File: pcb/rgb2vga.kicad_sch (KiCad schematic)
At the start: 40 parts, among them J1 GPIO_0, J2 RGB_IN, J3 COCO3_RGB_IN, J4 C_VIDEO_IN, J5 GPIO_1, J6 VGA_OUT, J7 Conn_01x03_Male, SW1 SW_DIP_x10, SW2 SW_DP3T, U1 LM1881

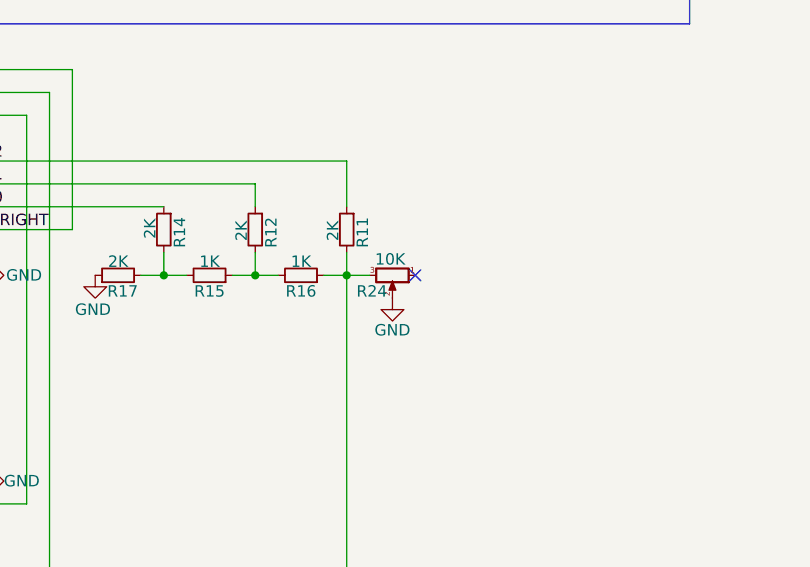
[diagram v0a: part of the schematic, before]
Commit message: multi-turn DAC trimmer pot
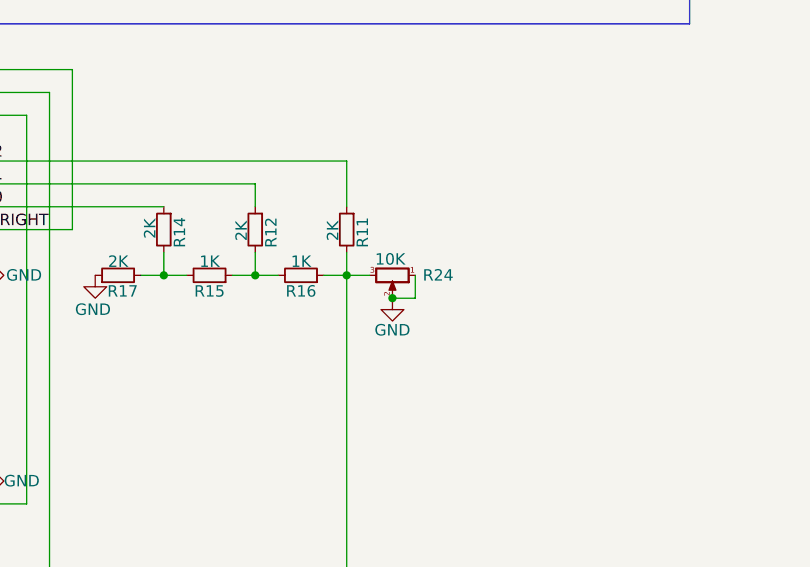
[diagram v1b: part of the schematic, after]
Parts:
- R24: footprint 000_LOCAL:PT10Lx-hole -> 000_LOCAL:Potentiometer_Bourns_3006P_Horizontal
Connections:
- net GND: now also R24.1
- no-connect marks 57 -> 56
